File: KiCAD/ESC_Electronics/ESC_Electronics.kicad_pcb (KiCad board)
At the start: 2 copper layers, 149.5 x 74.5 mm, 68 parts, among them J1 Batt probe, J10 RV Prob, J2 CA probe, J3 Test Input BNC, J4 -1000VDC SHV, J5 Output BNC, J6 Wire, J7 DC Power, J8 -8V, J9 +8V, U1 CR110, U2 SiPhotodiode, U3 TL051CP, U4 LM317L, U5 UA78M08, U6 UA79M08, U7 TLE2426xP

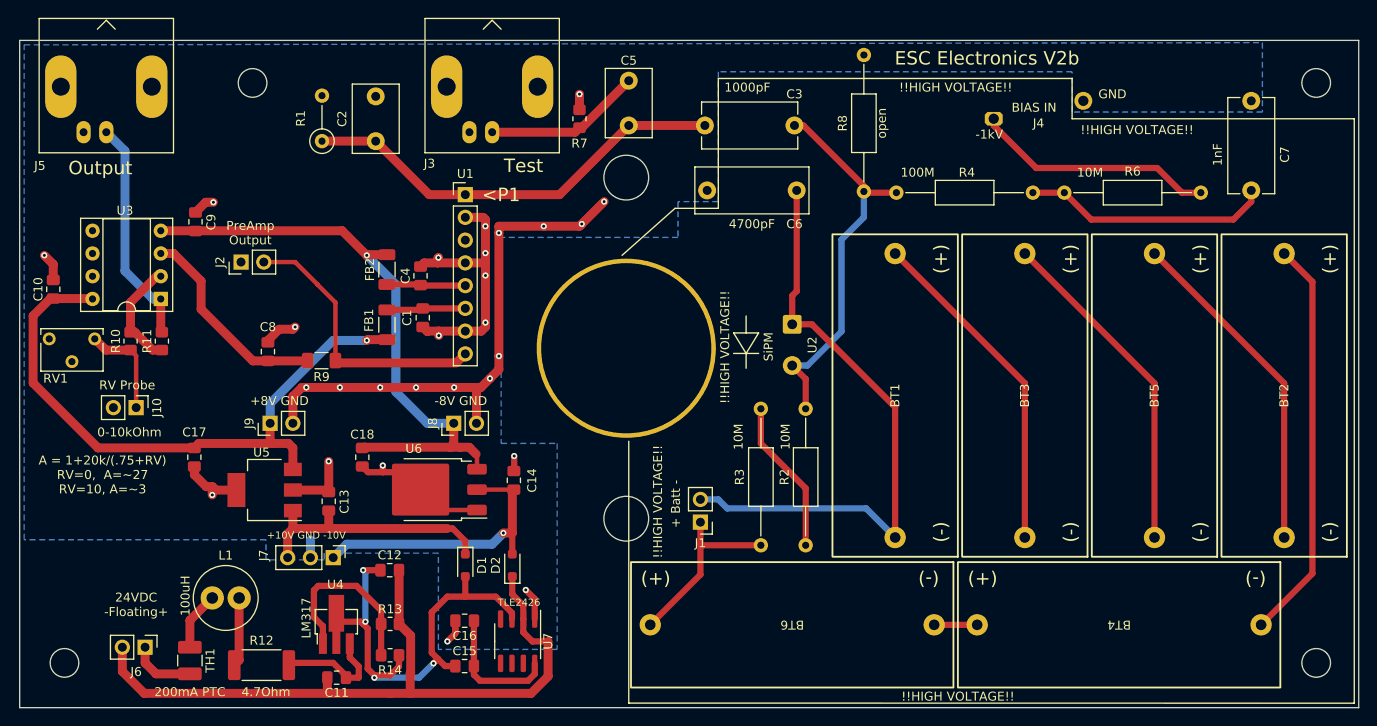
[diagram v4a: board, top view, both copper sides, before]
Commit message: Another mistake on the Neg8V resistor
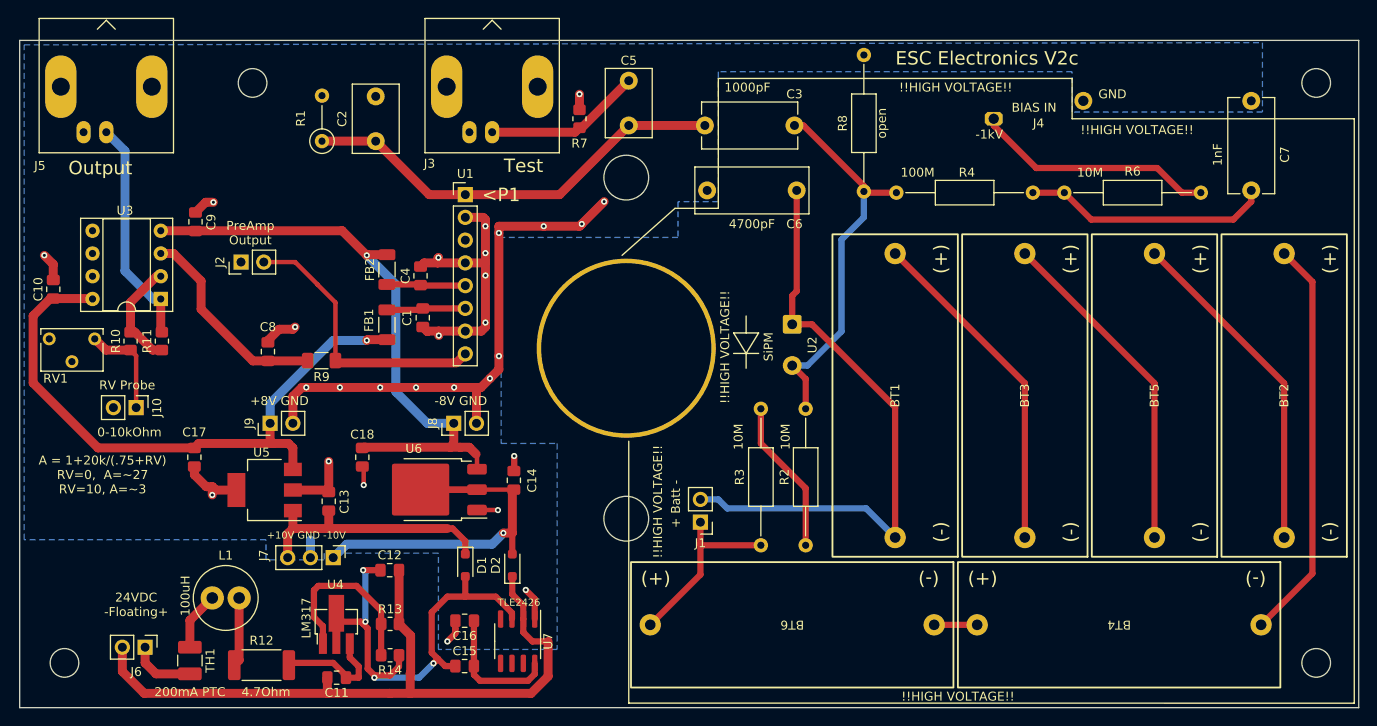
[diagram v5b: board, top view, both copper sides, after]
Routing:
- net GND: track 144.0 -> 131.2 mm, vias 27 -> 28
- net Net-(D2-A): track 32.3 -> 43.5 mm
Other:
- board text added: "ESC Electronics V2c"
- board text removed: "ESC Electronics V2b"
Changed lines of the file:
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@@
     (pad "1" smd roundrect (at -5.04 -2.28 180) (size 2.2 1.2) (layers "F.Cu" "F.Paste" "F.Mask") (roundrect_rratio 0.208333)
       (net 8 "GND") (pinfunction "GND") (pintype "power_in"))
-    (pad "1" smd roundrect (at 1.26 0 180) (size 6.4 5.8) (layers "F.Cu" "F.Mask") (roundrect_rratio 0.043103)
-      (net 8 "GND") (pinfunction "GND") (pintype "power_in"))
     (pad "2" smd roundrect (at -5.04 0 180) (size 2.2 1.2) (layers "F.Cu" "F.Paste" "F.Mask") (roundrect_rratio 0.208333)
+      (net 21 "Net-(D2-A)") (pinfunction "IN") (pintype "power_in"))
+    (pad "2" smd roundrect (at 1.26 0 180) (size 6.4 5.8) (layers "F.Cu" "F.Mask") (roundrect_rratio 0.043103)
       (net 21 "Net-(D2-A)") (pinfunction "IN") (pintype "power_in"))
     (pad "3" smd roundrect (at -5.04 2.28 180) (size 2.2 1.2) (layers "F.Cu" "F.Paste" "F.Mask") (roundrect_rratio 0.208333)
@@
     (effects (font (size 1.5 1.5) (thickness 0.3)))
   )
-  (gr_text "ESC Electronics V2b" (at 159 57) (layer "F.SilkS")
+  (gr_text "ESC Electronics V2c" (at 159 57) (layer "F.SilkS")
     (effects (font (size 1.5 1.5) (thickness 0.2)))
   )
@@
   (segment (start 127 111.25) (end 127 108.79) (width 0.7) (layer "F.Cu") (net 7))
   (segment (start 127.12 111.37) (end 127 111.25) (width 0.7) (layer "F.Cu") (net 7))
-  (segment (start 93.5625 103.2125) (end 93.98 103.63) (width 0.7) (layer "F.Cu") (net 8))
   (segment (start 106.2095 103.0435) (end 106.2095 101.406) (width 0.7) (layer "F.Cu") (net 8))
   (segment (start 79.9625 87.25) (end 81.5 87.25) (width 1) (layer "F.Cu") (net 8))
@@
   (segment (start 72.625 73.075) (end 71.7625 73.075) (width 1) (layer "F.Cu") (net 8))
   (segment (start 113.5 75.75) (end 113.75 75.5) (width 1) (layer "F.Cu") (net 8))
+  (segment (start 102.058 107.436) (end 104.388 107.436) (width 0.5) (layer "F.Cu") (net 8))
   (segment (start 85.45 105.2) (end 81.5 105.2) (width 1) (layer "F.Cu") (net 8))
   (segment (start 104.5 75.75) (end 109.5 75.75) (width 1) (layer "F.Cu") (net 8))
+  (segment (start 89.25 102.575) (end 89.408 102.733) (width 0.1524) (layer "F.Cu") (net 8))
   (segment (start 81.5 87.25) (end 81.75 87) (width 1) (layer "F.Cu") (net 8))
   (segment (start 95.25 93.75) (end 91.25 93.75) (width 1) (layer "F.Cu") (net 8))
-  (segment (start 93.8145 103.2125) (end 95.758 105.156) (width 0.7) (layer "F.Cu") (net 8))
   (segment (start 96.5 87.5) (end 96.54 87.46) (width 1) (layer "F.Cu") (net 8))
   (segment (start 103 86.5) (end 103 87) (width 1) (layer "F.Cu") (net 8))
@@
   (segment (start 99.642478 120.712573) (end 99.642478 121.212573) (width 0.7) (layer "F.Cu") (net 8))
   (segment (start 103 87) (end 102.54 87.46) (width 1) (layer "F.Cu") (net 8))
-  (segment (start 91.5375 103.2125) (end 91.5375 102.4625) (width 0.7) (layer "F.Cu") (net 8))
   (segment (start 104.5 91.75) (end 104.5 90.25) (width 1) (layer "F.Cu") (net 8))
   (segment (start 100.75 74.76) (end 102.74 74.76) (width 1) (layer "F.Cu") (net 8))
@@
   (segment (start 54.75 81.75) (end 54.75 80) (width 1) (layer "F.Cu") (net 8))
   (segment (start 102.74 74.76) (end 103 75.02) (width 1) (layer "F.Cu") (net 8))
-  (segment (start 98.085 107.435) (end 97.33 106.68) (width 0.5) (layer "F.Cu") (net 8))
-  (segment (start 91.5375 103.2125) (end 93.8145 103.2125) (width 0.7) (layer "F.Cu") (net 8))
-  (segment (start 98.038 107.436) (end 95.758 105.156) (width 0.5) (layer "F.Cu") (net 8))
   (segment (start 96.16 79.84) (end 95.75 80.25) (width 1) (layer "F.Cu") (net 8))
   (segment (start 70.5 103.5) (end 70.5 102.575) (width 1) (layer "F.Cu") (net 8))
@@
   (segment (start 72.5 104.825) (end 71.825 104.825) (width 1) (layer "F.Cu") (net 8))
   (segment (start 102.25 93.75) (end 102.5 93.75) (width 1) (layer "F.Cu") (net 8))
-  (segment (start 91.5375 103.2125) (end 89.8875 103.2125) (width 0.7) (layer "F.Cu") (net 8))
   (segment (start 113.75 75.5) (end 116.25 73) (width 1) (layer "F.Cu") (net 8))
   (segment (start 100 93.75) (end 99.5 93.75) (width 1) (layer "F.Cu") (net 8))
+  (segment (start 104.388 107.436) (end 104.394 107.442) (width 0.1524) (layer "F.Cu") (net 8))
   (segment (start 97.79 87.46) (end 97.79 87.96) (width 1) (layer "F.Cu") (net 8))
   (segment (start 78.7125 88.5) (end 79.9625 87.25) (width 1) (layer "F.Cu") (net 8))
@@
   (segment (start 96 87) (end 96.5 87.5) (width 1) (layer "F.Cu") (net 8))
   (segment (start 103.5 92.75) (end 104.5 91.75) (width 1) (layer "F.Cu") (net 8))
+  (segment (start 89.408 102.733) (end 89.408 104.648) (width 0.5) (layer "F.Cu") (net 8))
   (segment (start 85.5 102) (end 85.5 105.425) (width 1) (layer "F.Cu") (net 8))
   (segment (start 103 75.75) (end 103 78.75) (width 1) (layer "F.Cu") (net 8))
   (segment (start 97.66 79.84) (end 96.16 79.84) (width 1) (layer "F.Cu") (net 8))
   (segment (start 99.642478 119.796259) (end 99.642478 120.712573) (width 0.7) (layer "F.Cu") (net 8))
-  (segment (start 89.8875 103.2125) (end 89.25 102.575) (width 0.7) (layer "F.Cu") (net 8))
   (segment (start 71.7625 73.075) (end 70.625 74.2125) (width 1) (layer "F.Cu") (net 8))
   (segment (start 100.75 79.84) (end 97.66 79.84) (width 1) (layer "F.Cu") (net 8))
   (segment (start 71.825 104.825) (end 70.5 103.5) (width 1) (layer "F.Cu") (net 8))
   (segment (start 82.5 93.75) (end 81.5 94.75) (width 1) (layer "F.Cu") (net 8))
-  (segment (start 102.058 107.436) (end 98.038 107.436) (width 0.5) (layer "F.Cu") (net 8))
   (via (at 103 75.75) (size 0.6858) (drill 0.3302) (layers "F.Cu" "B.Cu") (net 8))
   (via (at 103 81.25) (size 0.6858) (drill 0.3302) (layers "F.Cu" "B.Cu") (net 8))
@@
   (via (at 97.75 79.25) (size 0.6858) (drill 0.3302) (layers "F.Cu" "B.Cu") (net 8))
   (via (at 103 86.5) (size 0.6858) (drill 0.3302) (layers "F.Cu" "B.Cu") (net 8))
+  (via (at 104.394 107.442) (size 0.6858) (drill 0.3302) (layers "F.Cu" "B.Cu") (free) (net 8))
   (via (at 85.5 102) (size 0.6858) (drill 0.3302) (layers "F.Cu" "B.Cu") (net 8))
+  (via (at 89.408 104.648) (size 0.6858) (drill 0.3302) (layers "F.Cu" "B.Cu") (free) (net 8))
   (via (at 106.2095 101.406) (size 0.6858) (drill 0.3302) (layers "F.Cu" "B.Cu") (net 8))
   (via (at 83 93.75) (size 0.6858) (drill 0.3302) (layers "F.Cu" "B.Cu") (net 8))
@@
   (via (at 72.5 105.75) (size 0.6858) (drill 0.3302) (layers "F.Cu" "B.Cu") (net 8))
   (via (at 91.25 93.75) (size 0.6858) (drill 0.3302) (layers "F.Cu" "B.Cu") (net 8))
-  (via (at 91.5375 102.4625) (size 0.6858) (drill 0.3302) (layers "F.Cu" "B.Cu") (net 8))
   (via (at 53.75 79) (size 0.6858) (drill 0.3302) (layers "F.Cu" "B.Cu") (net 8))
   (via (at 103 78.75) (size 0.6858) (drill 0.3302) (layers "F.Cu" "B.Cu") (net 8))
@@
   (segment (start 85.5 107.5) (end 85.5 109.5) (width 1) (layer "F.Cu") (net 20))
   (segment (start 81.5 109.5) (end 80.92 110.08) (width 1) (layer "F.Cu") (net 20))
+  (segment (start 93.5625 103.2125) (end 93.98 103.63) (width 0.7) (layer "F.Cu") (net 21))
   (segment (start 106 110) (end 105 110) (width 1) (layer "F.Cu") (net 21))
   (segment (start 106 112.355051) (end 106 110) (width 0.7) (layer "F.Cu") (net 21))
   (segment (start 102.058 105.156) (end 106.172 105.156) (width 0.5) (layer "F.Cu") (net 21))
+  (segment (start 98.085 107.435) (end 97.33 106.68) (width 0.5) (layer "F.Cu") (net 21))
+  (segment (start 102.058 105.156) (end 95.758 105.156) (width 0.75) (layer "F.Cu") (net 21))
+  (segment (start 98.038 107.436) (end 95.758 105.156) (width 0.5) (layer "F.Cu") (net 21))
   (segment (start 106 110) (end 106 105.328) (width 1) (layer "F.Cu") (net 21))
   (via (at 105 110) (size 0.6858) (drill 0.3302) (layers "F.Cu" "B.Cu") (net 21))

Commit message: Modification for external PS
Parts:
- removed the C15 at (100.7, 124.9)
- removed the C16 at (100.7, 119.8)
- removed the J6 at (65.0, 122.8)
- removed L1: L_Small, Inductor_THT:L_Radial_D7.0mm_P3.00mm
- removed R12: 4.7, Resistor_SMD:R_2512_6332Metric_Pad1.40x3.35mm_HandSolder
- removed R13: 7k, Resistor_SMD:R_0805_2012Metric_Pad1.20x1.40mm_HandSolder
- removed R14: 470, Resistor_SMD:R_0805_2012Metric_Pad1.20x1.40mm_HandSolder
- removed TH1: PTC 200mA, Fuse:Fuse_1210_3225Metric_Pad1.42x2.65mm_HandSolder
- removed the U4 at (86.3, 119.9)
- removed U7: TLE2426xP, Package_SO:SOIC-8_3.9x4.9mm_P1.27mm
- C11, C12: value 1uF -> 330uF; footprint Capacitor_SMD:C_0805_2012Metric_Pad1.18x1.45mm_HandSolder -> Capacitor_THT:CP_Radial_D10.0mm_P5.00mm
- D1, D2: footprint Diode_SMD:D_SOD-323_HandSoldering -> Diode_SMD:D_SOD-123
- J7: footprint Connector_PinHeader_2.54mm:PinHeader_1x03_P2.54mm_Vertical -> Connector_Molex:Molex_KK-254_AE-6410-03A_1x03_P2.54mm_Vertical
- moved D2 38.3 mm to (69.5, 125.0), turned to 0 degrees
- moved D1 31.7 mm to (69.2, 116.6), turned to 180 degrees
- moved J7 26.3 mm to (59.9, 116.6), turned to 90 degrees
- moved C11 10.4 mm to (80.8, 117.3), turned to -90 degrees
- moved C12 10.3 mm to (98.6, 122.3), turned to 90 degrees
- moved J2 3.24 mm to (78.2, 81.8)
- renumbered C17 to C15, C18 to C16, J10 to J5, J5 to J6, R11 to R10, R6 to R5, R7 to R6, R8 to R7, R9 to R8, R10 to R9, U5 to U4, U6 to U5
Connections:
- C11 pad 1: Net-(U4-VI) -> Net-(D1-K)
- C11 pad 2: Net-(D2-K) -> GND
- C12 pad 1: Net-(D1-A) -> GND
- C12 pad 2: Net-(D2-K) -> Net-(D2-A)
- J7 pad 1: Net-(D2-A) -> Net-(D2-K)
- J7 pad 3: Net-(D1-K) -> Net-(D1-A)
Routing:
- net Net-(D2-K): track 81.9 -> 12.8 mm
- net Net-(D1-A): track 53.3 -> 9.73 mm, vias 4 -> 0
- net Net-(U4-ADJ): track 19.9 -> 0.00 mm
- net Net-(D2-A): track 43.5 -> 63.0 mm, vias 1 -> 0
- net Net-(U7-NOISE_REDUCTION): track 14.6 -> 0.00 mm
- net Net-(U4-VI): track 13.2 -> 0.00 mm
- net Net-(L1-Pad2): track 7.73 -> 0.00 mm
- net Net-(J6-Pin_1): track 7.26 -> 0.00 mm
- net Net-(L1-Pad1): track 6.54 -> 0.00 mm
- net +8VDC: track 69.6 -> 73.4 mm, vias 1 -> 2
- net GND: track 131.2 -> 127.4 mm, vias 28 -> 36
- net -8VDC: track 68.6 -> 72.3 mm, vias 1 -> 3
- net Net-(J2-Pin_2): track 31.4 -> 28.3 mm
- net Net-(D1-K): track 28.8 -> 26.4 mm
- net Net-(J3-In): track 17.6 -> 18.4 mm
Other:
- board text added: "+12V"
- board text added: "-12V"
- board text removed: "+10V GND -10V"
- board text removed: "100uH"
- board text removed: "200mA PTC"
- board text removed: "24VDC -Floating+"
- board text removed: "4.7Ohm"
- board text removed: "LM317"
- board text removed: "TLE2426"

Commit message: added PTC to power input
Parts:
- added F1: Polyfuse_Small, Resistor_SMD:R_1210_3225Metric_Pad1.30x2.65mm_HandSolder, F.Cu at (66.8, 111.5)
- added F2: Polyfuse_Small, Resistor_SMD:R_1210_3225Metric_Pad1.30x2.65mm_HandSolder, F.Cu at (66.8, 120.9)
- moved J7 3.81 mm to (56.1, 116.6)
- moved D2 0.64 mm to (69.1, 125.5)
- moved D1 0.57 mm to (69.0, 116.1)
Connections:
- J7 pad 1: Net-(D2-K) -> Net-(J7-Pin_1)
- J7 pad 3: Net-(D1-A) -> Net-(J7-Pin_3)
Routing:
- net Net-(J7-Pin_1): track 0.00 -> 10.9 mm
- net Net-(J7-Pin_3): track 0.00 -> 9.09 mm
- net Net-(D2-K): track 12.8 -> 4.94 mm
- net GND: track 127.4 -> 134.2 mm, vias 36 -> 39
- net Net-(D1-A): track 9.73 -> 4.99 mm
- net Net-(D2-A): track 63.0 -> 63.6 mm
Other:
- board text added: "ESC Electronics V3"
- board text added: "PTC 100mA"
- board text removed: "ESC Electronics V2c"
